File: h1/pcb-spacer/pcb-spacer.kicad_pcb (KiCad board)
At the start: 2 copper layers, 92.7 x 126.6 mm, 7 parts, among them J1 Conn_01x01_Pin

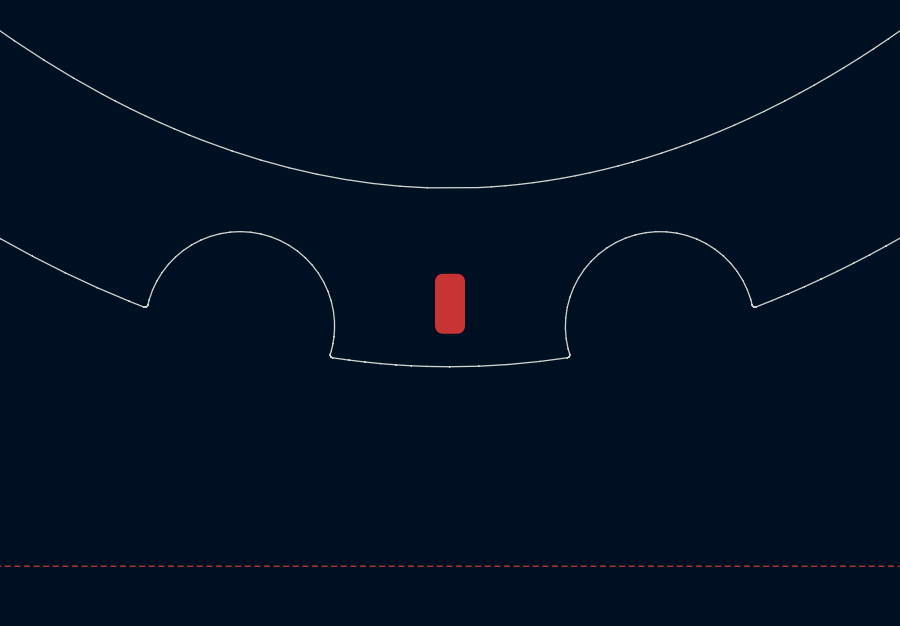
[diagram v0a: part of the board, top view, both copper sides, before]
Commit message: h1: move spacer solder point outwards
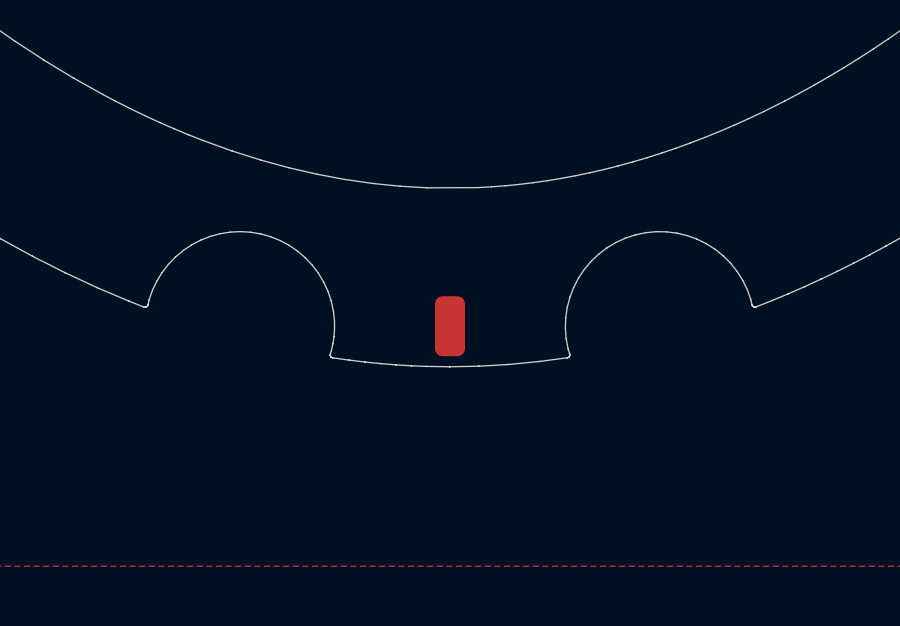
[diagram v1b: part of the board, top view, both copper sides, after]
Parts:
- moved J1 0.75 mm to (100.0, 162.0)
